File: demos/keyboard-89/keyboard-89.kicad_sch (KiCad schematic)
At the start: 178 parts

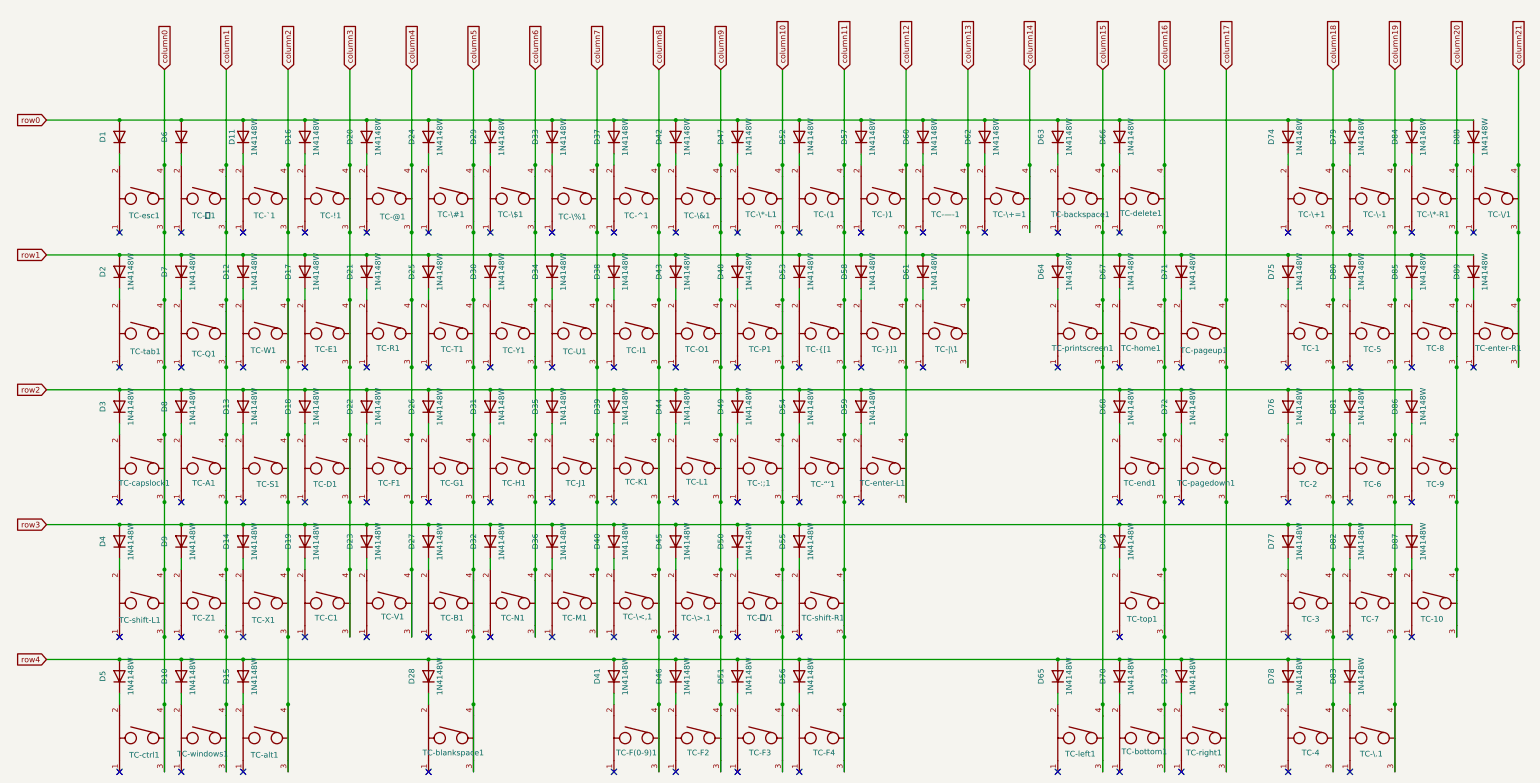
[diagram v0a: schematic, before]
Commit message: Add new footprints for various components in keyboard-89 project
- Added C_0402_1005Metric footprint for 0402 capacitors.
- Added C_0805_2012Metric footprint for 0805 capacitors.
- Added Crystal_YSX321SL footprint for YSX321SL crystals.
- Added D_SOD-123 footprint for SOD-123 diodes.
- Added PinHeader_1x05_P2.54mm_Vertical footprint for 1x05 SWD headers.
- Added QFN-56-1EP_7x7mm_P0.4mm_EP3.2x3.2mm footprint for RP2040 QFN-56 packages.
- Added R_0402_1005Metric footprint for 0402 resistors.
- Added SOIC-8_3.9x4.9mm_P1.27mm footprint for JEDEC MS-012AA SOIC-8 packages.
- Added SOT-89-3 footprint for AMS1117-3.3.
- Added TC-6601-5-160G footprint for 6x6 mm tactile switches.
- Added USB_C_16P_2MD_073 footprint for TYPE-C connectors.
- Created keyboard_controller schematic file for the keyboard-89 project.
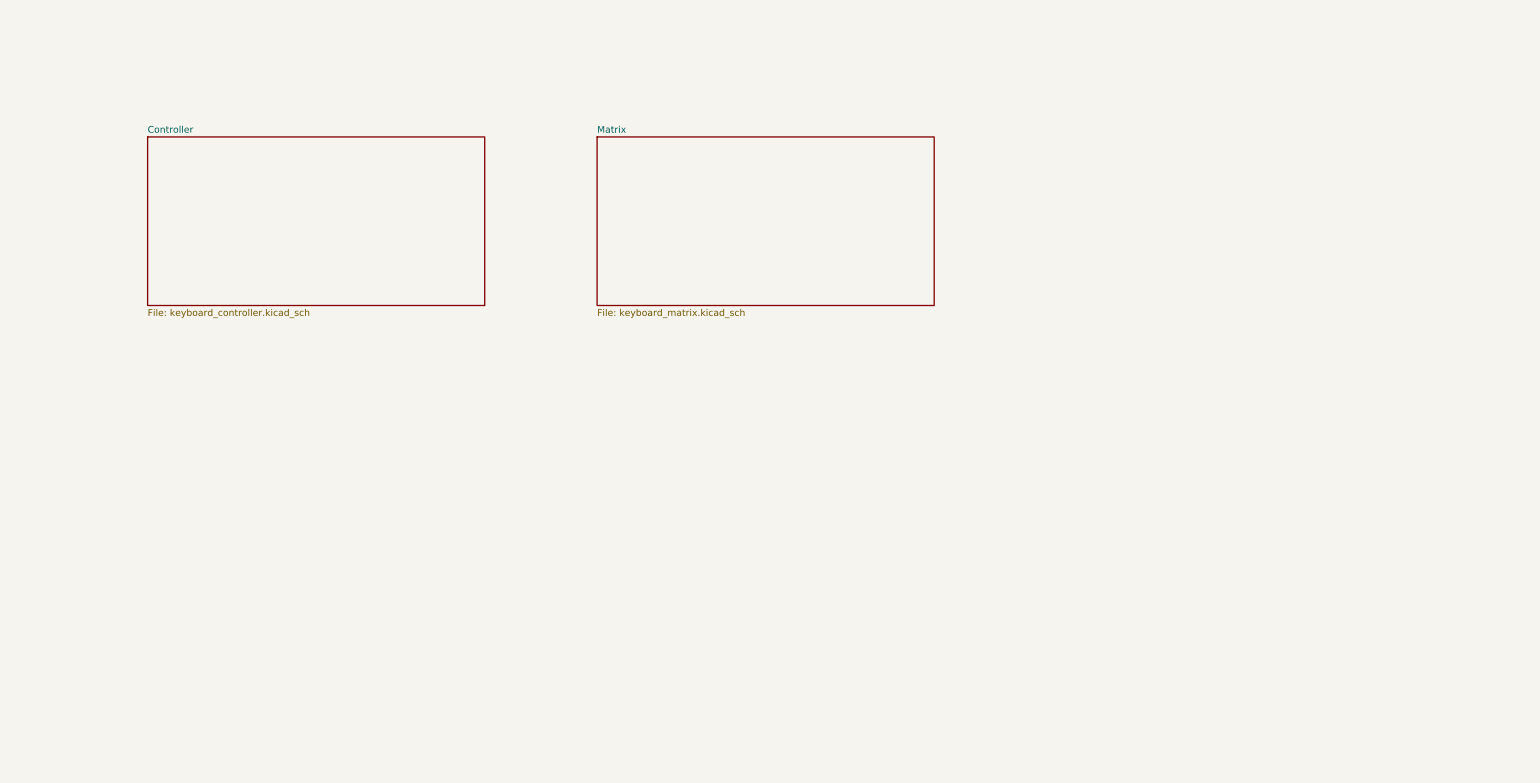
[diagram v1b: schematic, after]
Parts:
- removed D1, D10, D11, D12, D13, D14, D15, D16, D17, D18, D19, D2, D20, D21, D22, D23, D24, D25, D26, D27, D28, D29, D3, D30, D31, D32, D33, D34, D35, D36, D37, D38, D39, D4, D40, D41, D42, D43, D44, D45, D46, D47, D48, D49, D5, D50, D51, D52, D53, D54, D55, D56, D57, D58, D59, D6, D60, D61, D62, D63, D64, D65, D66, D67, D68, D69, D7, D70, D71, D72, D73, D74, D75, D76, D77, D78, D79, D8, D80, D81, D82, D83, D84, D85, D86, D87, D88, D89, D9: 1N4148W, Diode_SMD:D_SOD-123, symbol Diode:1N4148W
- removed TC-!1, TC-(1, TC-)1, TC-1, TC-10, TC-2, TC-3, TC-4, TC-5, TC-6, TC-7, TC-8, TC-9, TC-:;1, TC-@1, TC-A1, TC-B1, TC-C1, TC-D1, TC-E1, TC-F(0-9)1, TC-F1, TC-F2, TC-F3, TC-F4, TC-G1, TC-H1, TC-I1, TC-J1, TC-K1, TC-L1, TC-M1, TC-N1, TC-O1, TC-P1, TC-Q1, TC-R1, TC-S1, TC-T1, TC-U1, TC-V1, TC-W1, TC-X1, TC-Y1, TC-Z1, TC-\#1, TC-\$1, TC-\%1, TC-\&1, TC-\*-L1, TC-\*-R1, TC-\+1, TC-\+=1, TC-\-1, TC-\.1, TC-\/1, TC-\<,1, TC-\>.1, TC-^1, TC-`1, TC-alt1, TC-backspace1, TC-blankspace1, TC-bottom1, TC-capslock1, TC-ctrl1, TC-delete1, TC-end1, TC-enter-L1, TC-enter-R1, TC-esc1, TC-home1, TC-left1, TC-pagedown1, TC-pageup1, TC-printscreen1, TC-right1, TC-shift-L1, TC-shift-R1, TC-tab1, TC-top1, TC-windows1, TC-{[1, TC-|\1, TC-}]1, TC-—-1, TC-“‘1, TC-？/1, TC-～1: (no value), symbol private_lib:TC-6601-5-160G
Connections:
- no-connect marks 89 -> 0
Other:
- added sheet Controller (keyboard_controller.kicad_sch)
- added sheet Matrix (keyboard_matrix.kicad_sch)
- company: 卢占辉 -> Keyboard-89
- title: 按键原理图 -> Keyboard-89 Production Schematic

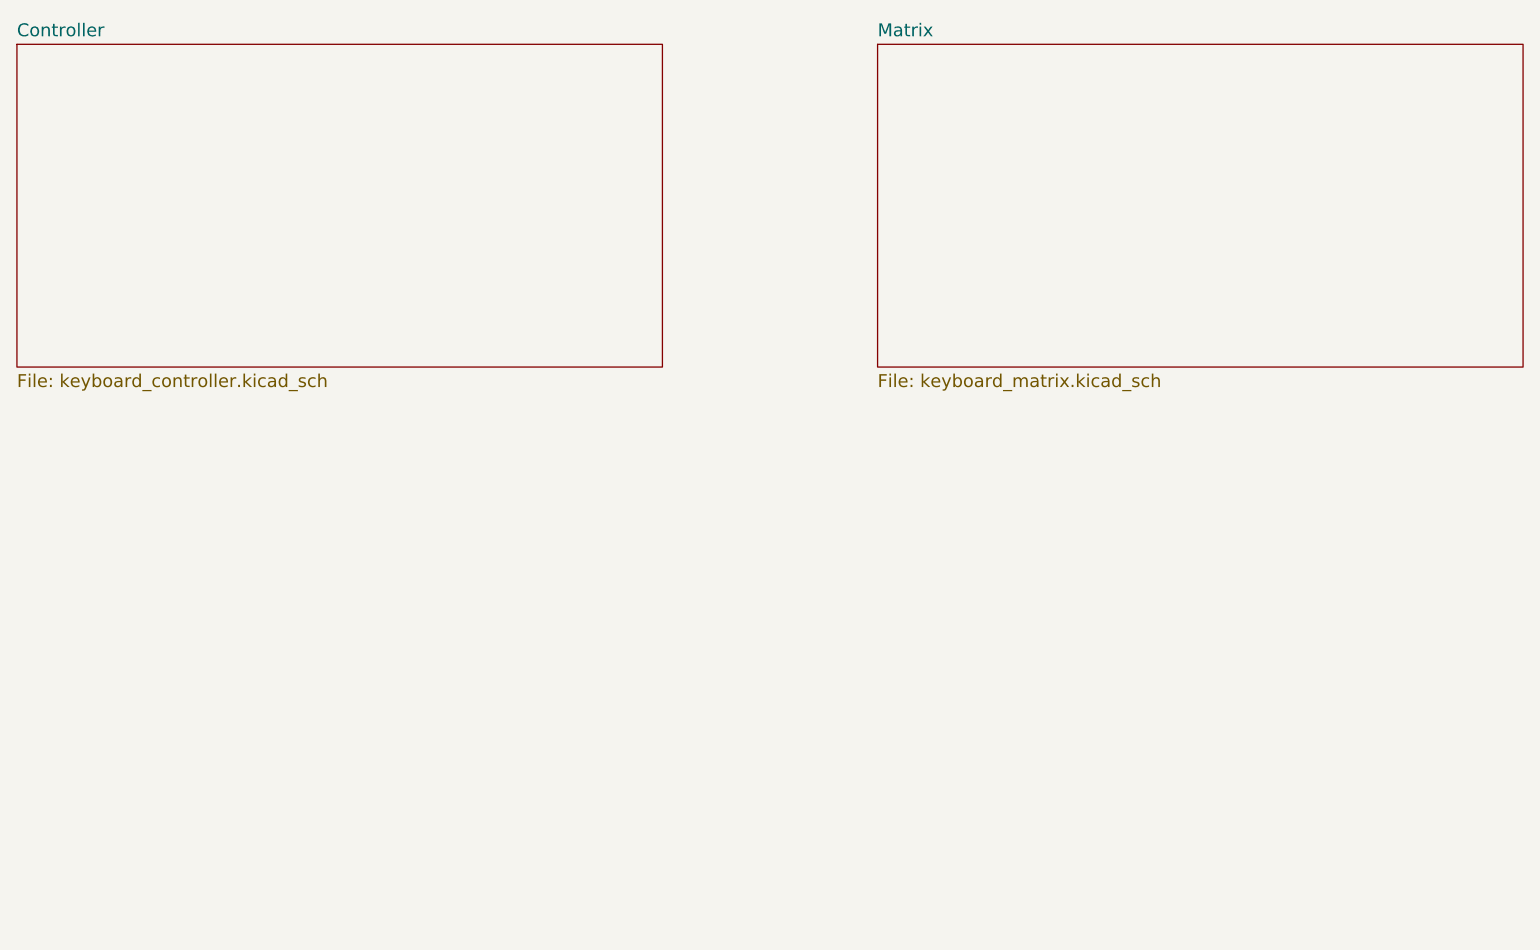
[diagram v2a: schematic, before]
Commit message: Add ERC report, AI setup documentation, and bootstrap scripts
- Created a new ERC report for the keyboard-89 project detailing isolated pin labels and library issues.
- Added AI environment bootstrap documentation for setting up the development environment on Windows and Linux.
- Implemented a PowerShell bootstrap script for Windows to automate the setup of dependencies, environment, and build process.
- Developed a corresponding bash bootstrap script for Linux with similar functionality.
- Introduced a new test for verifying pin connections in the symbol writer module.
- Added JSON report for failed drawing processes with a specific error message in Chinese.
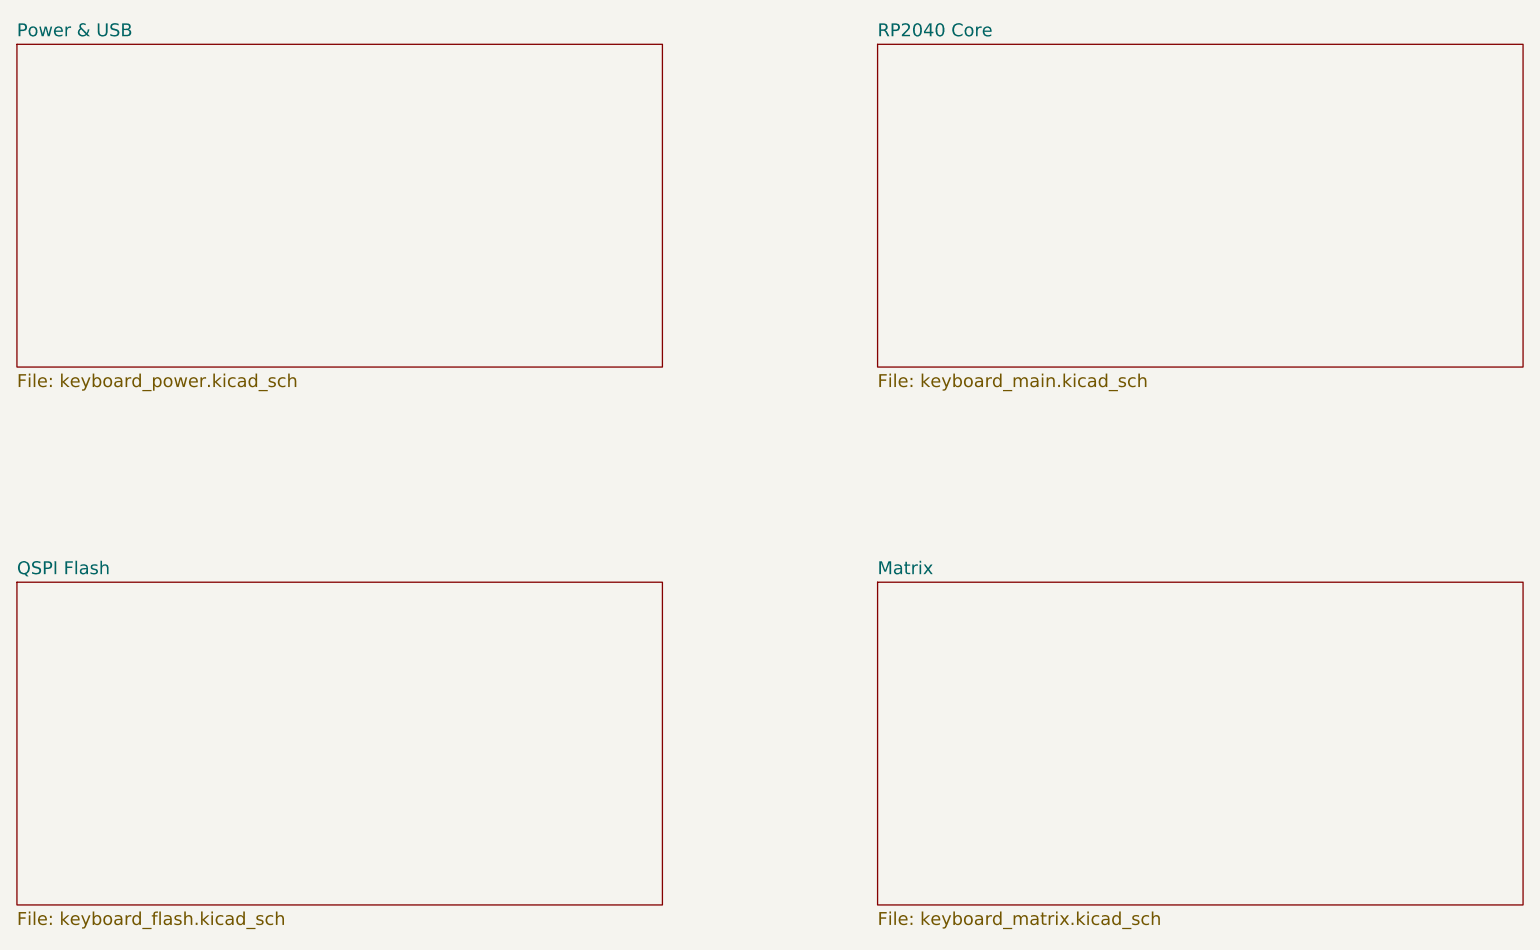
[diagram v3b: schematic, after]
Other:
- sheet Controller renamed Power & USB
- added sheet QSPI Flash (keyboard_flash.kicad_sch)
- added sheet RP2040 Core (keyboard_main.kicad_sch)
- sheet Power & USB: file keyboard_controller.kicad_sch -> keyboard_power.kicad_sch
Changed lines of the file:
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@@
 	(generator "eeschema")
 	(generator_version "10.0")
-	(paper "A4")
+	(paper "A3")
 	(title_block
 		(title "Keyboard-89 Production Schematic")
 		(date "2026-08-30")
-		(rev "1.0")
+		(rev "2.0")
 		(company "Keyboard-89")
-		(comment 1 "RP2040 controller and 5x22 sparse matrix, 89 keys")
+		(comment 1 "USB-C, RP2040, QSPI and 5x22 sparse matrix, 89 keys")
 	)
 	(sheet
@@
 			(color 0 0 0 0)
 		)
-		(property "Sheetname" "Controller"
+		(property "Sheetname" "Power & USB"
 			(at 50.8 50.0375 0)
 			(show_name no)
@@
 			)
 		)
-		(property "Sheetfile" "keyboard_controller.kicad_sch"
+		(property "Sheetfile" "keyboard_power.kicad_sch"
 			(at 50.8 89.6625 0)
 			(show_name no)
@@
 			(project "keyboard-89"
 				(path "/90509e26-8ec4-4712-b0e0-6bdb2801d7c5"
-					(page "4")
+					(page "6")
+				)
+			)
+		)
+	)
+	(sheet
+		(at 152.4 114.3)
+		(size 76.2 38.1)
+		(exclude_from_sim no)
+		(in_bom yes)
+		(on_board yes)
+		(dnp no)
+		(fields_autoplaced yes)
+		(stroke
+			(width 0)
+			(type solid)
+		)
+		(fill
+			(color 0 0 0 0)
+		)
+		(property "Sheetname" "Matrix"
+			(at 152.4 113.5375 0)
+			(show_name no)
+			(do_not_autoplace no)
+			(effects
+				(font
+					(size 1.524 1.524)
+				)
+				(justify left bottom)
+			)
+		)
+		(property "Sheetfile" "keyboard_matrix.kicad_sch"
+			(at 152.4 153.1625 0)
+			(show_name no)
+			(do_not_autoplace no)
+			(effects
+				(font
+					(size 1.524 1.524)
+				)
+				(justify left top)
+			)
+		)
+		(instances
+			(project "keyboard-89"
+				(path "/90509e26-8ec4-4712-b0e0-6bdb2801d7c5"
+					(page "5")
 				)
 			)
@@
 			(color 0 0 0 0)
 		)
-		(property "Sheetname" "Matrix"
+		(property "Sheetname" "RP2040 Core"
 			(at 152.4 50.0375 0)
 			(show_name no)
@@
 			)
 		)
-		(property "Sheetfile" "keyboard_matrix.kicad_sch"
+		(property "Sheetfile" "keyboard_main.kicad_sch"
 			(at 152.4 89.6625 0)
 			(show_name no)
@@
 			(project "keyboard-89"
 				(path "/90509e26-8ec4-4712-b0e0-6bdb2801d7c5"
-					(page "5")
+					(page "7")
 				)
 			)
+		)
+	)
+	(sheet
+		(at 50.8 114.3)
+		(size 76.2 38.1)
+		(exclude_from_sim no)
+		(in_bom yes)
+		(on_board yes)
+		(dnp no)
+		(fields_autoplaced yes)
+		(stroke
+			(width 0)
+			(type solid)
+		)
+		(fill
+			(color 0 0 0 0)
+		)
+		(property "Sheetname" "QSPI Flash"
+			(at 50.8 113.5375 0)
+			(show_name no)
+			(do_not_autoplace no)
+			(effects
+				(font
+					(size 1.524 1.524)
+				)
+				(justify left bottom)
+			)
+		)
+		(property "Sheetfile" "keyboard_flash.kicad_sch"
+			(at 50.8 153.1625 0)
+			(show_name no)
+			(do_not_autoplace no)
+			(effects
+				(font
+					(size 1.524 1.524)
+				)
+				(justify left top)
+			)
+		)
+		(instances
+			(project "keyboard-89"
+				(path "/90509e26-8ec4-4712-b0e0-6bdb2801d7c5"
+					(page "4")
+				)
+			)
